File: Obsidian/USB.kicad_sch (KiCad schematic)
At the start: 40 parts, among them J2 USB_C_Receptacle_USB2.0_16P, U21 FT2232HQ, U22 93C46B-I_SN, U8 TLV62565DBV, Y5 XTAL_12MHZ_TXC_7A-12.000MAAJ-T

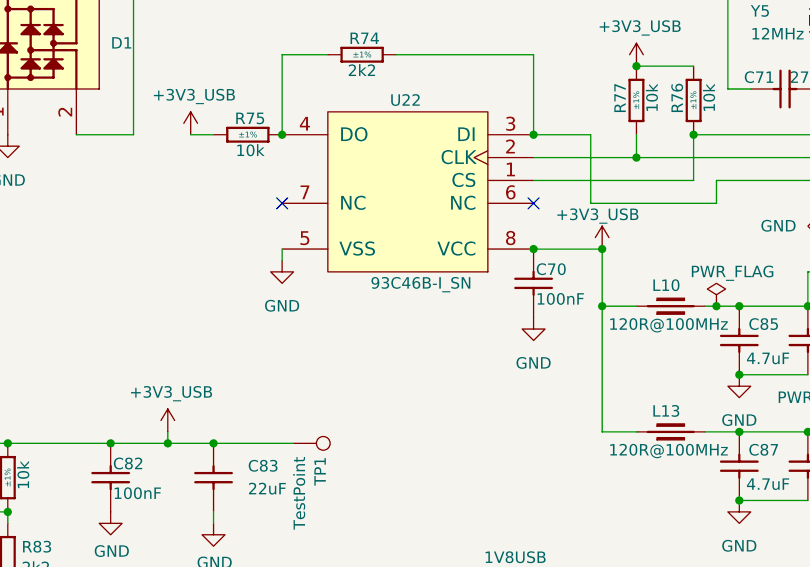
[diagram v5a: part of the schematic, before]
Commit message: correcting some footprint issues
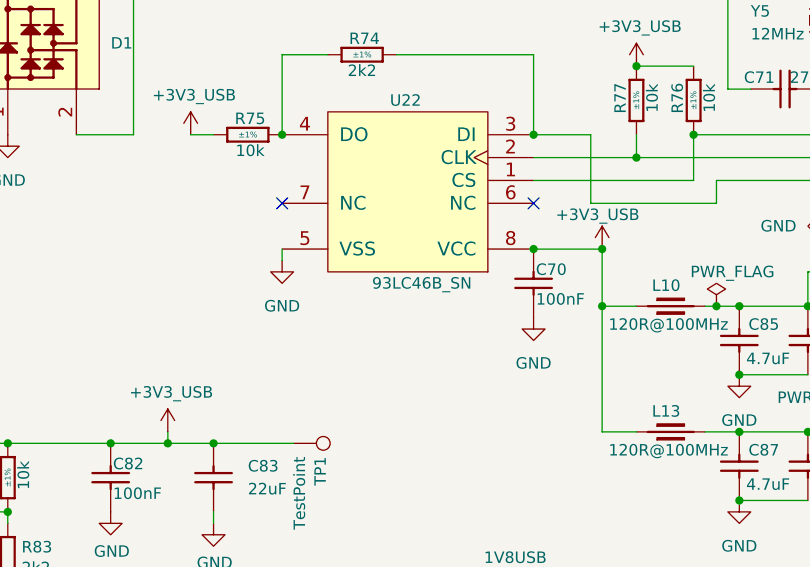
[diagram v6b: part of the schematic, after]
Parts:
- U22: value 93C46B-I_SN -> 93LC46B_SN
- Y5: value XTAL_12MHZ_TXC_7A-12.000MAAJ-T -> X503212MSB2GI; Part Number XTAL_12MHZ_TXC_7A-12.000MAAJ-T -> X503212MSB2GI
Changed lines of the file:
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@@
 			)
 		)
-		(property "Value" "XTAL_12MHZ_TXC_7A-12.000MAAJ-T"
+		(property "Value" "X503212MSB2GI"
 			(at 174.625 66.04 0)
 			(effects
@@
 			)
 		)
-		(property "Part Number" "XTAL_12MHZ_TXC_7A-12.000MAAJ-T"
+		(property "Part Number" "X503212MSB2GI"
 			(at 168.91 66.04 0)
 			(effects
@@
 			)
 		)
-		(property "Value" "93C46B-I_SN"
+		(property "Value" "93LC46B_SN"
 			(at 141.732 91.44 0)
 			(effects
